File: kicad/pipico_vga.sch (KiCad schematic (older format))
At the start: 47 parts, among them J1 Conn_01x15, J2 DB15_Male_HighDensity_Mountin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, U1 Pico, U2 74LVC162244ADGVJ

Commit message: progress on pcb rev2
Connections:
- net +3V3: now also J1.11 (Pin_11); no longer J1.5 (Pin_5)
- net gpio0: now also U2.22 (4y2); no longer U2.2 (1y0)
- net gpio1: now also U2.20 (4y1); no longer U2.3 (1y1)
- net gpio10: now also U2.8 (2y0); no longer U2.16 (3y2)
- net gpio11: now also U2.6 (1y3); no longer U2.17 (3y3)
- net gpio12: now also U2.5 (1y2); no longer U2.19 (4y0)
- net gpio13: now also U2.3 (1y1); no longer U2.20 (4y1)
- net gpio14: now also U2.2 (1y0); no longer U2.22 (4y2)
- net gpio2: now also U2.19 (4y0); no longer U2.5 (1y2)
- net gpio3: now also U2.17 (3y3); no longer U2.6 (1y3)
- net gpio4: now also U2.16 (3y2); no longer U2.8 (2y0)
- net gpio5: now also U2.14 (3y1); no longer U2.9 (2y1)
- net gpio6: now also U2.13 (3y0); no longer U2.11 (2y2)
- net gpio8: now also U2.11 (2y2); no longer U2.13 (3y0)
- net gpio9: now also U2.9 (2y1); no longer U2.14 (3y1)
- net hsync: now also U1.21 (GPIO16); no longer U1.25 (GPIO19)
- net vga_clk: now also U1.25 (GPIO19); no longer U1.22 (GPIO17)
- net vga_data: now also U1.24 (GPIO18); no longer U1.21 (GPIO16)
- net vsync: now also U1.22 (GPIO17); no longer U1.24 (GPIO18)
- net b4: now reaches U2.40 (2a1)
- net b4: now also R28.2; no longer R2.2
- net b3: now reaches U2.38 (2a2)
- net b3: now also R27.2; no longer R3.2
- net b2: now reaches U2.37 (2a3)
- net b2: now also R26.2; no longer R4.2
- net b1: now reaches U2.36 (3a0)
- net b1: now also R25.2; no longer R5.2
- net b0: now reaches U2.35 (3a1)
- net b0: now also R24.2; no longer R6.2
- net at U1.26 (GPIO20): now also J1.1 (Pin_1); no longer J1.15 (Pin_15)
- net at U1.27 (GPIO21): now also J1.2 (Pin_2); no longer J1.14 (Pin_14)
- net at U1.29 (GPIO22): now also J1.4 (Pin_4); no longer J1.12 (Pin_12)
- net at U1.30 (RUN): now also J1.5 (Pin_5); no longer J1.11 (Pin_11)
- net at U1.31 (GPIO26_ADC0): now also J1.6 (Pin_6); no longer J1.10 (Pin_10)
- net at U1.32 (GPIO27_ADC1): now also J1.7 (Pin_7); no longer J1.9 (Pin_9)
- net at U1.34 (GPIO28_ADC2): now also J1.9 (Pin_9); no longer J1.7 (Pin_7)
- net at U1.35 (ADC_VREF): now also J1.10 (Pin_10); no longer J1.6 (Pin_6)
- net at U1.37 (3V3_EN): now also J1.12 (Pin_12); no longer J1.4 (Pin_4)
- net at U1.39 (VSYS): now also J1.14 (Pin_14); no longer J1.2 (Pin_2)
- net at U1.40 (VBUS): now also J1.15 (Pin_15); no longer J1.1 (Pin_1)
- net r0: now reaches R13.2
- net r0: now also U2.27 (4a2); no longer U2.33 (3a2)
- net r1: now reaches R14.2
- net r1: now also U2.29 (4a1); no longer U2.32 (3a3)
- net r2: now reaches R15.2, U2.30 (4a0)
- net r3: now reaches R16.2
- net r3: now also U2.32 (3a3); no longer U2.29 (4a1)
- net r4: now reaches R17.2
- net r4: now also U2.33 (3a2); no longer U2.27 (4a2)
- net g4: now reaches U2.47 (1a0)
- net g4: now also R6.2; no longer R24.2
- net g3: now reaches U2.46 (1a1)
- net g3: now also R5.2; no longer R25.2
- net g2: now reaches U2.44 (1a2)
- net g2: now also R4.2; no longer R26.2
- net g1: now reaches U2.43 (1a3)
- net g1: now also R3.2; no longer R27.2
- net g0: now reaches U2.41 (2a0)
- net g0: now also R2.2; no longer R28.2
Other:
- moved on the sheet: J1, J2, R1, R10, R11, R12, R13, R14, R15, R16, R17, R18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

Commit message: Add v2 PCB
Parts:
- TP1, TP2, TP3, TP4, TP5, TP6: footprint TestPoint:TestPoint_Pad_D1.5mm -> TestPoint:TestPoint_THTPad_D2.0mm_Drill1.0mm
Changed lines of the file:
@@
 F 0 "TP6" V 9354 5188 50  0000 L CNN
 F 1 "TestPoint" V 9445 5188 50  0000 L CNN
-F 2 "TestPoint:TestPoint_Pad_D1.5mm" H 9600 5000 50  0001 C CNN
+F 2 "TestPoint:TestPoint_THTPad_D2.0mm_Drill1.0mm" H 9600 5000 50  0001 C CNN
 F 3 "~" H 9600 5000 50  0001 C CNN
 	1    9400 5000
@@
 F 0 "TP5" V 9354 4988 50  0000 L CNN
 F 1 "TestPoint" V 9445 4988 50  0000 L CNN
-F 2 "TestPoint:TestPoint_Pad_D1.5mm" H 9600 4800 50  0001 C CNN
+F 2 "TestPoint:TestPoint_THTPad_D2.0mm_Drill1.0mm" H 9600 4800 50  0001 C CNN
 F 3 "~" H 9600 4800 50  0001 C CNN
 	1    9400 4800
@@
 F 0 "TP4" V 9354 4788 50  0000 L CNN
 F 1 "TestPoint" V 9445 4788 50  0000 L CNN
-F 2 "TestPoint:TestPoint_Pad_D1.5mm" H 9600 4600 50  0001 C CNN
+F 2 "TestPoint:TestPoint_THTPad_D2.0mm_Drill1.0mm" H 9600 4600 50  0001 C CNN
 F 3 "~" H 9600 4600 50  0001 C CNN
 	1    9400 4600
@@
 F 0 "TP3" V 9354 4488 50  0000 L CNN
 F 1 "TestPoint" V 9445 4488 50  0000 L CNN
-F 2 "TestPoint:TestPoint_Pad_D1.5mm" H 9600 4300 50  0001 C CNN
+F 2 "TestPoint:TestPoint_THTPad_D2.0mm_Drill1.0mm" H 9600 4300 50  0001 C CNN
 F 3 "~" H 9600 4300 50  0001 C CNN
 	1    9400 4300
@@
 F 0 "TP2" V 9354 4288 50  0000 L CNN
 F 1 "TestPoint" V 9445 4288 50  0000 L CNN
-F 2 "TestPoint:TestPoint_Pad_D1.5mm" H 9600 4100 50  0001 C CNN
+F 2 "TestPoint:TestPoint_THTPad_D2.0mm_Drill1.0mm" H 9600 4100 50  0001 C CNN
 F 3 "~" H 9600 4100 50  0001 C CNN
 	1    9400 4100
@@
 F 0 "TP1" V 9354 4088 50  0000 L CNN
 F 1 "TestPoint" V 9445 4088 50  0000 L CNN
-F 2 "TestPoint:TestPoint_Pad_D1.5mm" H 9600 3900 50  0001 C CNN
+F 2 "TestPoint:TestPoint_THTPad_D2.0mm_Drill1.0mm" H 9600 3900 50  0001 C CNN
 F 3 "~" H 9600 3900 50  0001 C CNN
 	1    9400 3900

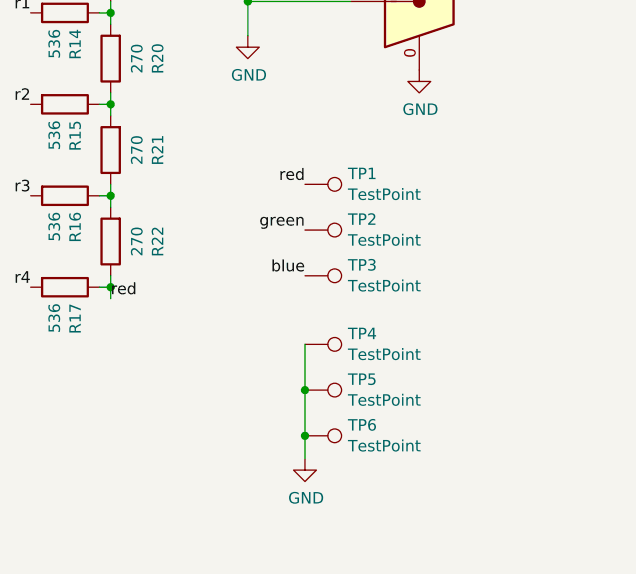
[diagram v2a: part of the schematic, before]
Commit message: Add mounting hole
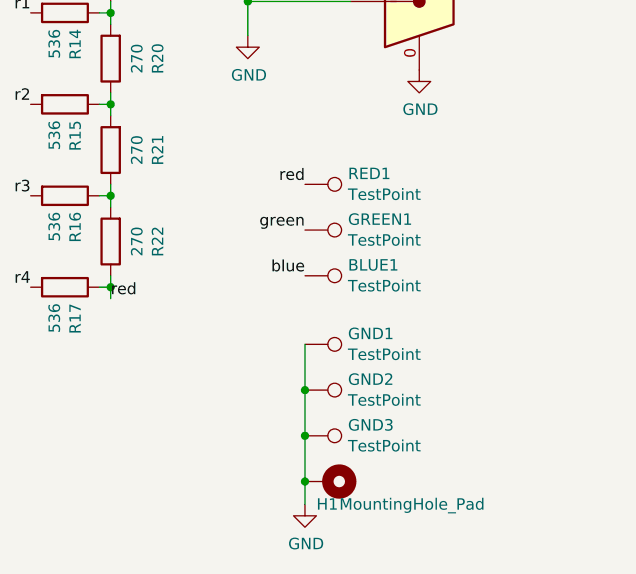
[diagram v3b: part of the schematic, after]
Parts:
- added H1: MountingHole_Pad, MountingHole:MountingHole_3.2mm_M3_Pad, symbol Mechanical:MountingHole_Pad
- renumbered TP3 to BLUE1, TP4 to GND1, TP5 to GND2, TP6 to GND3, TP2 to GREEN1, TP1 to RED1
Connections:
- net GND: now also H1.1
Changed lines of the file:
@@
 Connection ~ 9400 5000
-Wire Wire Line
-	9400 5100 9400 5000
-$Comp
-L power:GND #PWR0101
-U 1 1 602AB62B
-P 9400 5100
-F 0 "#PWR0101" H 9400 4850 50  0001 C CNN
-F 1 "GND" H 9405 4927 50  0000 C CNN
-F 2 "" H 9400 5100 50  0001 C CNN
-F 3 "" H 9400 5100 50  0001 C CNN
-	1    9400 5100
-	1    0    0    -1
-$EndComp
 Wire Wire Line
 	9400 4800 9400 5000
@@
 	9400 4600 9400 4800
 $Comp
-L Connector:TestPoint TP6
+L Connector:TestPoint GND3
 U 1 1 602A27FA
 P 9400 5000
-F 0 "TP6" V 9354 5188 50  0000 L CNN
+F 0 "GND3" V 9354 5188 50  0000 L CNN
 F 1 "TestPoint" V 9445 5188 50  0000 L CNN
 F 2 "TestPoint:TestPoint_THTPad_D2.0mm_Drill1.0mm" H 9600 5000 50  0001 C CNN
@@
 $EndComp
 $Comp
-L Connector:TestPoint TP5
+L Connector:TestPoint GND2
 U 1 1 602A27F4
 P 9400 4800
-F 0 "TP5" V 9354 4988 50  0000 L CNN
+F 0 "GND2" V 9354 4988 50  0000 L CNN
 F 1 "TestPoint" V 9445 4988 50  0000 L CNN
 F 2 "TestPoint:TestPoint_THTPad_D2.0mm_Drill1.0mm" H 9600 4800 50  0001 C CNN
@@
 $EndComp
 $Comp
-L Connector:TestPoint TP4
+L Connector:TestPoint GND1
 U 1 1 602A27EE
 P 9400 4600
-F 0 "TP4" V 9354 4788 50  0000 L CNN
+F 0 "GND1" V 9354 4788 50  0000 L CNN
 F 1 "TestPoint" V 9445 4788 50  0000 L CNN
 F 2 "TestPoint:TestPoint_THTPad_D2.0mm_Drill1.0mm" H 9600 4600 50  0001 C CNN
@@
 $EndComp
 $Comp
-L Connector:TestPoint TP3
+L Connector:TestPoint BLUE1
 U 1 1 6027BD8F
 P 9400 4300
-F 0 "TP3" V 9354 4488 50  0000 L CNN
+F 0 "BLUE1" V 9354 4488 50  0000 L CNN
 F 1 "TestPoint" V 9445 4488 50  0000 L CNN
 F 2 "TestPoint:TestPoint_THTPad_D2.0mm_Drill1.0mm" H 9600 4300 50  0001 C CNN
@@
 $EndComp
 $Comp
-L Connector:TestPoint TP2
+L Connector:TestPoint GREEN1
 U 1 1 6027B902
 P 9400 4100
-F 0 "TP2" V 9354 4288 50  0000 L CNN
+F 0 "GREEN1" V 9354 4288 50  0000 L CNN
 F 1 "TestPoint" V 9445 4288 50  0000 L CNN
 F 2 "TestPoint:TestPoint_THTPad_D2.0mm_Drill1.0mm" H 9600 4100 50  0001 C CNN
@@
 $EndComp
 $Comp
-L Connector:TestPoint TP1
+L Connector:TestPoint RED1
 U 1 1 6027B3D3
 P 9400 3900
-F 0 "TP1" V 9354 4088 50  0000 L CNN
+F 0 "RED1" V 9354 4088 50  0000 L CNN
 F 1 "TestPoint" V 9445 4088 50  0000 L CNN
 F 2 "TestPoint:TestPoint_THTPad_D2.0mm_Drill1.0mm" H 9600 3900 50  0001 C CNN
@@
 Text Label 5700 2950 0    50   ~ 0
 b4
+$Comp
+L Mechanical:MountingHole_Pad H1
+U 1 1 605442D5
+P 9500 5200
+F 0 "H1" V 9600 5150 50  0000 L CNN
+F 1 "MountingHole_Pad" V 9600 5250 50  0000 L CNN
+F 2 "MountingHole:MountingHole_3.2mm_M3_Pad" H 9500 5200 50  0001 C CNN
+F 3 "~" H 9500 5200 50  0001 C CNN
+	1    9500 5200
+	0    1    1    0
+$EndComp
+Wire Wire Line
+	9400 5000 9400 5200
+$Comp
+L power:GND #PWR0101
+U 1 1 605791B2
+P 9400 5300
+F 0 "#PWR0101" H 9400 5050 50  0001 C CNN
+F 1 "GND" H 9405 5127 50  0000 C CNN
+F 2 "" H 9400 5300 50  0001 C CNN
+F 3 "" H 9400 5300 50  0001 C CNN
+	1    9400 5300
+	1    0    0    -1
+$EndComp
+Wire Wire Line
+	9400 5300 9400 5200
+Connection ~ 9400 5200
 $EndSCHEMATC

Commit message: Rev3 pcb now correct footprint of buffer
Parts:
- C1, C2, C3, C4: footprint Capacitor_SMD:C_0805_2012Metric_Pad1.15x1.40mm_HandSolder -> Capacitor_SMD:C_0603_1608Metric_Pad1.05x0.95mm_HandSolder
- U1: symbol MCU_RaspberryPi_and_Boards:Pico -> pipico_vga-rescue:Pico-MCU_RaspberryPi_and_Boards
- U2: footprint Package_SO:TSSOP-48_6.1x12.5mm_P0.5mm -> good_things:SOIC-48; symbol random_things:74LVC162244ADGVJ -> pipico_vga-rescue:74LVC162244ADGVJ-random_things
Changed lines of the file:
@@
 F 0 "C1" H 5415 1646 50  0000 L CNN
 F 1 "100n" H 5415 1555 50  0000 L CNN
-F 2 "Capacitor_SMD:C_0805_2012Metric_Pad1.15x1.40mm_HandSolder" H 5338 1450 50  0001 C CNN
+F 2 "Capacitor_SMD:C_0603_1608Metric_Pad1.05x0.95mm_HandSolder" H 5338 1450 50  0001 C CNN
 F 3 "~" H 5300 1600 50  0001 C CNN
 	1    5300 1600
@@
 F 0 "C2" H 5815 1646 50  0000 L CNN
 F 1 "100n" H 5815 1555 50  0000 L CNN
-F 2 "Capacitor_SMD:C_0805_2012Metric_Pad1.15x1.40mm_HandSolder" H 5738 1450 50  0001 C CNN
+F 2 "Capacitor_SMD:C_0603_1608Metric_Pad1.05x0.95mm_HandSolder" H 5738 1450 50  0001 C CNN
 F 3 "~" H 5700 1600 50  0001 C CNN
 	1    5700 1600
@@
 F 0 "C3" H 6215 1646 50  0000 L CNN
 F 1 "100n" H 6215 1555 50  0000 L CNN
-F 2 "Capacitor_SMD:C_0805_2012Metric_Pad1.15x1.40mm_HandSolder" H 6138 1450 50  0001 C CNN
+F 2 "Capacitor_SMD:C_0603_1608Metric_Pad1.05x0.95mm_HandSolder" H 6138 1450 50  0001 C CNN
 F 3 "~" H 6100 1600 50  0001 C CNN
 	1    6100 1600
@@
 F 0 "C4" H 6615 1646 50  0000 L CNN
 F 1 "100n" H 6615 1555 50  0000 L CNN
-F 2 "Capacitor_SMD:C_0805_2012Metric_Pad1.15x1.40mm_HandSolder" H 6538 1450 50  0001 C CNN
+F 2 "Capacitor_SMD:C_0603_1608Metric_Pad1.05x0.95mm_HandSolder" H 6538 1450 50  0001 C CNN
 F 3 "~" H 6500 1600 50  0001 C CNN
 	1    6500 1600
@@
 g4
 $Comp
-L MCU_RaspberryPi_and_Boards:Pico U1
+L pipico_vga-rescue:Pico-MCU_RaspberryPi_and_Boards U1
 U 1 1 6020A685
 P 2300 3400
@@
 b0
 $Comp
-L random_things:74LVC162244ADGVJ U2
+L pipico_vga-rescue:74LVC162244ADGVJ-random_things U2
 U 1 1 60279B05
 P 5100 3450
 F 0 "U2" H 5100 5031 50  0000 C CNN
 F 1 "74LVC162244ADGVJ" H 5100 4940 50  0000 C CNN
-F 2 "Package_SO:TSSOP-48_6.1x12.5mm_P0.5mm" H 5500 4350 50  0001 C CNN
+F 2 "good_things:SOIC-48" H 5500 4350 50  0001 C CNN
 F 3 "" H 5500 4350 50  0001 C CNN
 	1    5100 3450

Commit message: Rev3 pcb and initial SW
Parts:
- removed BLUE1, GREEN1, RED1: TestPoint, TestPoint:TestPoint_THTPad_D2.0mm_Drill1.0mm, symbol Connector:TestPoint
- removed J1: Conn_01x15, Connector_PinHeader_2.54mm:PinHeader_1x15_P2.54mm_Vertical, symbol Connector_Generic:Conn_01x15
- removed R11, R22, R33: 270, Resistor_SMD:R_0603_1608Metric_Pad1.05x0.95mm_HandSolder, symbol Device:R
- removed R17, R28, R6: 536, Resistor_SMD:R_0603_1608Metric_Pad1.05x0.95mm_HandSolder, symbol Device:R
- added C5: 10u 18v, Capacitor_SMD:C_1206_3216Metric, symbol Device:C_Small
- added C6: 100n, Capacitor_SMD:C_0603_1608Metric_Pad1.05x0.95mm_HandSolder, symbol Device:C_Small
- added C7, C8: 22u 5v, Capacitor_SMD:C_0603_1608Metric_Pad1.05x0.95mm_HandSolder, symbol Device:C_Small
- added D1: BZT52C5V1+, Diode_SMD:D_SOD-123, symbol Device:D_Zener_Small
- added D2: RSX301L-30TE25, good_things:SOD-106, symbol Device:D_Schottky
- added F1: MC36232, Fuse:Fuse_1812_4532Metric, symbol Device:Fuse_Small
- added H2, H3, H4: MountingHole_Pad, MountingHole:MountingHole_3.2mm_M3_DIN965_Pad, symbol Mechanical:MountingHole_Pad
- added J1: RJ45_LED_Shielded, Connector_RJ:RJ45_BEL_SS74301-00x_Vertical, symbol Connector:RJ45_LED_Shielded
- added J3: power, TerminalBlock_Phoenix:TerminalBlock_Phoenix_MKDS-1,5-2_1x02_P5.00mm_Horizontal, symbol Connector_Generic:Conn_01x02
- added L1: 2u2, good_things:smd_inductor_0806_2016metric, symbol Device:L_Small
- added Q1, Q2: 2N7002P, Package_TO_SOT_SMD:SOT-23_Handsoldering, symbol Device:Q_NMOS_GSD
- added Q3: CPH3350-TL-W, Package_TO_SOT_SMD:SOT-23_Handsoldering, symbol Device:Q_PMOS_GSD
- added R28, R29: 1k, Resistor_SMD:R_0603_1608Metric_Pad1.05x0.95mm_HandSolder, symbol Device:R_Small
- added R30, R32: 10k, Resistor_SMD:R_0603_1608Metric_Pad1.05x0.95mm_HandSolder, symbol Device:R_Small
- added R31: 52k3, Resistor_SMD:R_0603_1608Metric_Pad1.05x0.95mm_HandSolder, symbol Device:R_Small
- added TP1: red, TestPoint:TestPoint_THTPad_D2.0mm_Drill1.0mm, symbol Connector:TestPoint
- added TP2: green, TestPoint:TestPoint_THTPad_D2.0mm_Drill1.0mm, symbol Connector:TestPoint
- added TP3: blue, TestPoint:TestPoint_THTPad_D2.0mm_Drill1.0mm, symbol Connector:TestPoint
- added TP4: hsync, TestPoint:TestPoint_THTPad_D2.0mm_Drill1.0mm, symbol Connector:TestPoint
- added TP5: vsync, TestPoint:TestPoint_THTPad_D2.0mm_Drill1.0mm, symbol Connector:TestPoint
- added TP6: 5v, TestPoint:TestPoint_Pad_D2.0mm, symbol Connector:TestPoint
- added U3: AP62250, Package_TO_SOT_SMD:TSOT-23-6, symbol good_things:AP62250
- H1: footprint MountingHole:MountingHole_3.2mm_M3_Pad -> MountingHole:MountingHole_3.2mm_M3_DIN965_Pad
- J2: footprint random_stuff:DSUB-15-HDEX15SNT -> good_things:DSUB-15-HDEX15SNT
- renumbered R23 to R1, R1 to R10, R2 to R11, R3 to R12, R4 to R13, R5 to R14, R7 to R15, R8 to R16, R9 to R17, R10 to R18, R12 to R19, R24 to R2, R13 to R20, R14 to R21, R15 to R22, R16 to R23, R18 to R24, R19 to R25, R20 to R26, R21 to R27, R25 to R3, R26 to R4, R27 to R5, R29 to R6, R30 to R7, R31 to R8, R32 to R9
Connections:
- net g4 is gone; now on net g3: U2.47 (1a0)
- net r4 is gone; now on net r1: U2.33 (3a2)
- net +3V3: now also J1.10, J1.12, J1.3
- net GND: now also U2.11 (2y2), U2.12 (2y3), U2.8 (2y0), U2.9 (2y1), C5.2, C7.2, C8.2, H2.1, H3.1, H4.1, J1.8, J1.SH, J3.1 (Pin_1), Q1.2 (S), Q2.2 (S), R30.2, R32.2, U3.1 (gnd); no longer U2.1 (~1oe), U2.23 (4y3), U2.24 (~4oe), U2.25 (~3oe), U2.48 (~2oe)
- net b0: now also U2.26 (4a3); no longer U2.35 (3a1)
- net b1: now also U2.27 (4a2); no longer U2.36 (3a0)
- net b2: now also U2.29 (4a1); no longer U2.37 (2a3)
- net b3: now also U2.30 (4a0); no longer U2.38 (2a2)
- net blue: now also R5.1, R9.1, TP3.1
- net g0: now also U2.43 (1a3); no longer U2.41 (2a0)
- net g1: now also U2.44 (1a2); no longer U2.43 (1a3)
- net g2: now also U2.46 (1a1); no longer U2.44 (1a2)
- net g3: no longer U2.46 (1a1)
- net green: now also R14.1, R18.1, TP2.1
- net hsync: now also U1.19 (GPIO14), TP4.1; no longer U1.21 (GPIO16)
- net r0: now also U2.32 (3a3); no longer U2.27 (4a2)
- net r1: no longer U2.29 (4a1)
- net r2: now also U2.35 (3a1); no longer U2.30 (4a0)
- net r3: now also U2.36 (3a0); no longer U2.32 (3a3)
- net red: now also R23.1, R27.1, TP1.1
- net vsync: now also U1.17 (GPIO13), TP5.1; no longer U1.22 (GPIO17)
- net connected: now reaches U1.26 (GPIO20)
- net connected: now also J1.7
- net led1: now reaches U1.27 (GPIO21)
- net led1: now also Q2.1 (G)
- net led0: now reaches U1.29 (GPIO22)
- net led0: now also Q1.1 (G)
- net at U1.39 (VSYS): now also D2.1 (K)
- net b4: no longer names the net of U2.40 (2a1)
- net gpio0 renamed pio_b0
- net pio_b0: now also U2.23 (4y3); no longer U2.22 (4y2)
- net gpio1 renamed pio_b1
- net pio_b1: now also U2.22 (4y2); no longer U2.20 (4y1)
- net gpio10 renamed pio_g2
- net pio_g2: now also U2.3 (1y1); no longer U2.8 (2y0)
- net gpio11 renamed pio_g0
- net pio_g0: now also U1.11 (GPIO8); no longer U1.15 (GPIO11)
- net gpio12 renamed pio_g1
- net pio_g1: now also U1.12 (GPIO9); no longer U1.16 (GPIO12)
- removed net gpio13: U1.17 (GPIO13), U2.3 (1y1)
- net gpio14 renamed pio_g3
- net pio_g3: now also U1.15 (GPIO11); no longer U1.19 (GPIO14)
- net gpio2 renamed pio_b2
- net pio_b2: now also U2.20 (4y1); no longer U2.19 (4y0)
- net gpio3 renamed pio_b3
- net pio_b3: now also U2.19 (4y0); no longer U2.17 (3y3)
- net gpio4 renamed pio_r0
- net pio_r0: now also U2.17 (3y3); no longer U2.16 (3y2)
- net gpio5 renamed pio_r1
- net pio_r1: now also U2.16 (3y2); no longer U2.14 (3y1)
- net gpio6 renamed pio_r2
- net pio_r2: now also U2.14 (3y1); no longer U2.13 (3y0)
- net gpio7 renamed pio_r3
- net pio_r3: now also U2.13 (3y0); no longer U2.12 (2y3)
- removed net gpio8: U1.11 (GPIO8), U2.11 (2y2)
- removed net gpio9: U1.12 (GPIO9), U2.9 (2y1)
- new net: J1.11, R28.1
- new net: J1.9, R29.1
- new net: Q2.3 (D), R28.2
- new net: Q1.3 (D), R29.2
- new net: D1.2 (A), Q3.1 (G), R30.1
- new net: F1.2, Q3.3 (D)
- new net: C6.1, U3.6 (bst)
- new net +5V: C7.1, C8.1, D2.2 (A), L1.2, R31.1, TP6.1
- new net rgb_oe: U1.16 (GPIO12), U2.1 (~1oe), U2.24 (~4oe), U2.25 (~3oe), U2.48 (~2oe)
- new net rx: J1.2, U1.22 (GPIO17)
- new net tx: J1.1, U1.21 (GPIO16)
- new net vin: C5.1, D1.1 (K), Q3.2 (S), U3.3 (vin)
- new net vin_raw: F1.1, J3.2 (Pin_2)
- new net vsys_fb: R31.2, R32.1, U3.4 (fb)
- new net vsys_sw: C6.2, L1.1, U3.2 (sw)
- no-connect marks 6 -> 10
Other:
- note added: "work with 16 bit words\n(order is not important)\nbit 0: ctrl\nbit 1: oe\nbit 2: hsync\nbit 3: vsync\nbit 4-7: r\nbit 8-11: g\nbit 12-15: b"
- moved on the sheet: U1
